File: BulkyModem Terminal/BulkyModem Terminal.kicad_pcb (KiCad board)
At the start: 2 copper layers, 100 x 100 mm, 79 parts, among them J1 DC IN, J2 RS-232, J3 Module_Panel, J4 VGA, J5 TTL, J6 PS/2_Connector, M1 Mounting, M2 Mounting, M3 Mounting, M4 Mounting, Q1 2N3904, Q2 2N7000, Q3 2N7000, SW1 RESET, SW2 DEFAULTS, U1 Pico, U2 74HCT244, U3 MAX232, U5 74HCT04

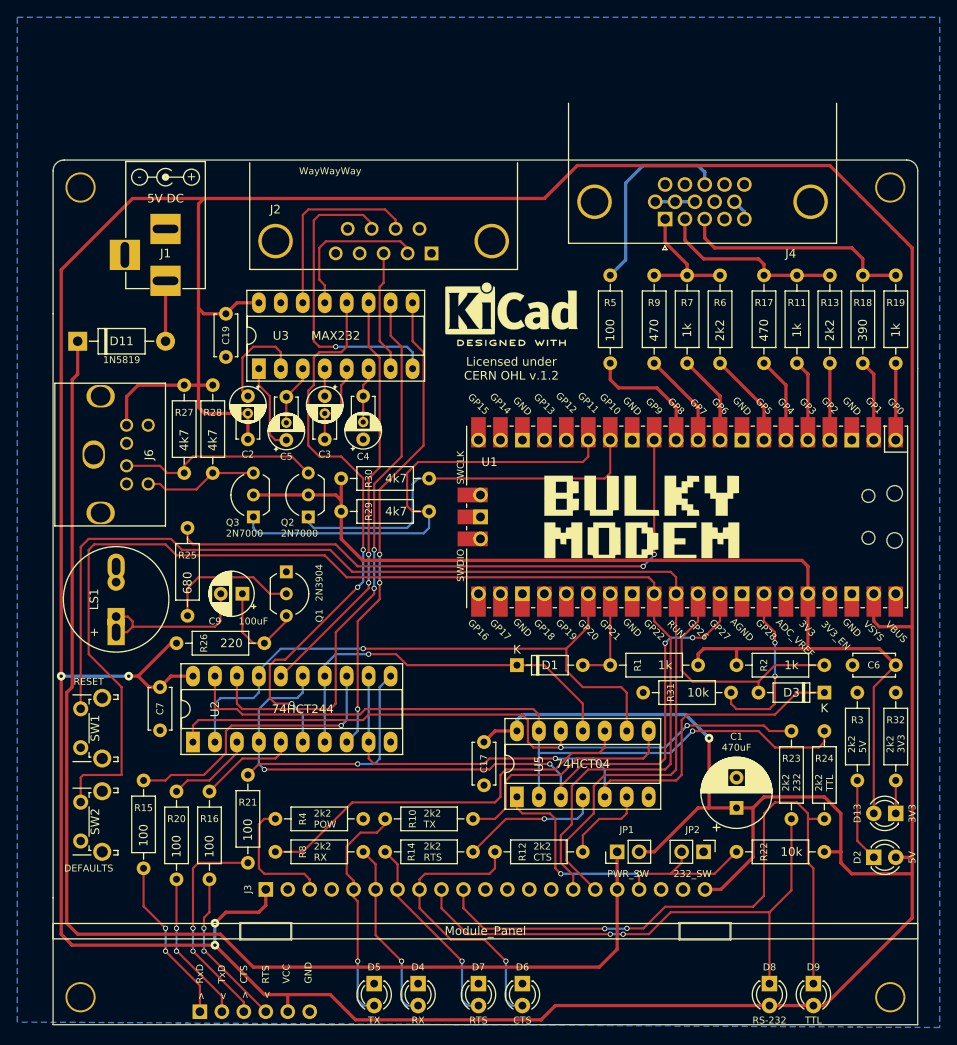
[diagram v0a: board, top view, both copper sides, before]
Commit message: Move PS/2 port to the back with some caveats, basically needs a custom top panel
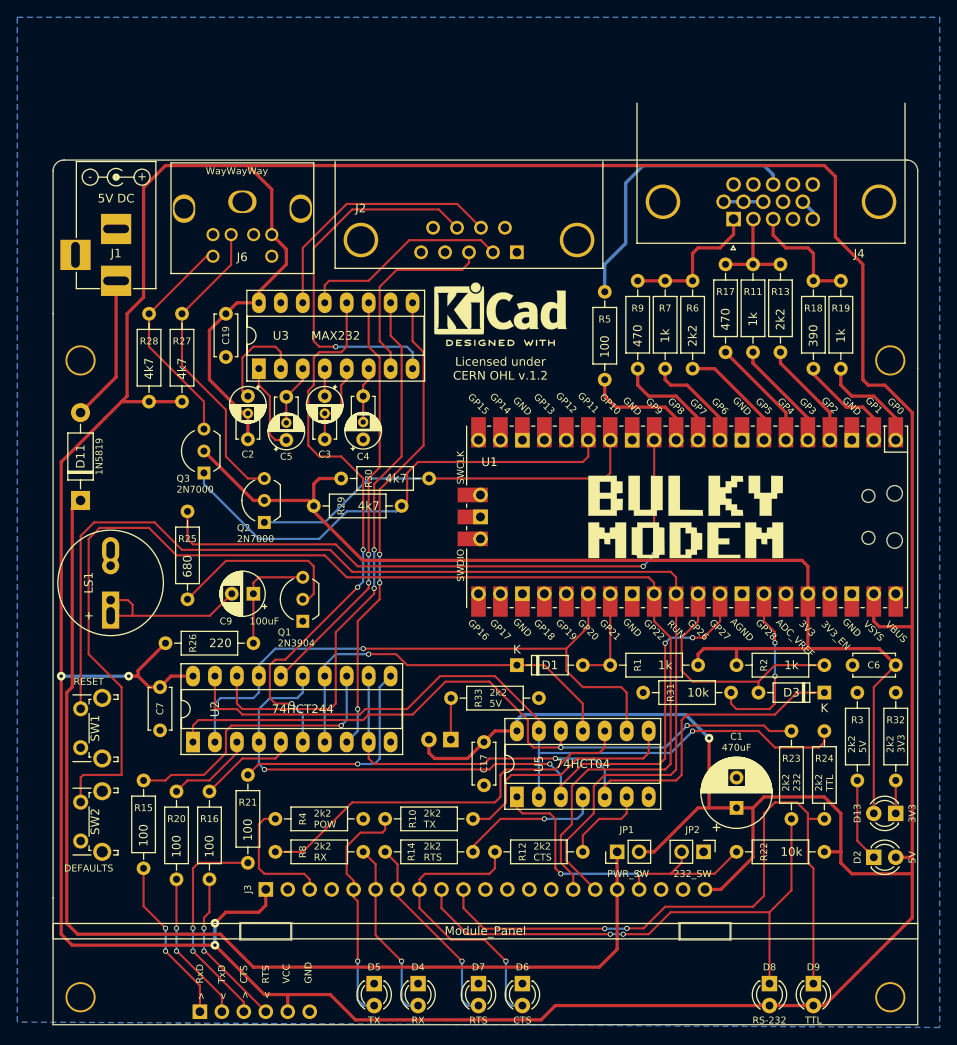
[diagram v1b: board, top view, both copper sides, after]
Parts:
- added D10: 5V, LED_THT:LED_D3.0mm_Horizontal_O1.27mm_Z2.0mm, B.Cu at (116.2, 121.6)
- added R33: 2k2, resistor:R_Axial_DIN0207_L6.3mm_D2.5mm_P10.16mm_Horizontal, F.Cu at (126.4, 116.8)
- moved J6 40.4 mm to (92.1, 54.7), turned to 0 degrees
- moved M3 20.0 mm to (167.0, 77.8)
- moved M4 20.0 mm to (73.4, 77.8)
- moved D11 18.4 mm to (73.4, 94.0), turned to 90 degrees
- moved J2 9.88 mm to (123.8, 65.3)
- moved J4 7.92 mm to (153.2, 48.0)
- moved Q3 7.65 mm to (87.6, 90.8)
- moved R28 7.61 mm to (81.3, 82.5), turned to 90 degrees
- moved R19 6.38 mm to (161.3, 78.7)
- moved Q1 6.02 mm to (99.1, 108.0), turned to 90 degrees
- moved R13 5.85 mm to (154.3, 76.8)
- moved R18 5.75 mm to (158.1, 78.7)
- moved J1 5.72 mm to (77.5, 68.6)
- moved SYM1 5.72 mm to (77.5, 56.5)
- moved R11 5.24 mm to (151.1, 76.8)
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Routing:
- net VIN: track 145.7 -> 127.4 mm
- net /VGA/VGA.B: track 26.7 -> 13.7 mm
- net Net-(Q3-D): track 13.2 -> 26.1 mm
- net Net-(Q2-D): track 23.5 -> 35.6 mm
- net Net-(J4-Pad13): track 22.6 -> 33.0 mm
- net Net-(D11-A): track 6.98 -> 16.9 mm
- net /VGA/VGA.G: track 21.1 -> 11.5 mm
- net +3.3V: track 127.5 -> 136.5 mm
- net /Serial/DTE.CTS: track 35.2 -> 43.9 mm
- net /Serial/DTE.TxD: track 14.1 -> 22.7 mm
- net /Serial/DTE.RTS: track 22.7 -> 30.2 mm
- net /Serial/DTE.RxD: track 18.1 -> 24.2 mm
- net Net-(Q1-B): track 15.3 -> 20.8 mm
- net Net-(D10-K): track 0.00 -> 4.80 mm
- net G0: track 8.89 -> 12.5 mm
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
